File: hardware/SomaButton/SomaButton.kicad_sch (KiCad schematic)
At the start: 18 parts, among them J1 LED+, J2 LED GND, J3 BTN GND, J4 I2C, J5 V12, J6 Buttons, J7 V5, U2 ULN2803A, U3 ULN2803A

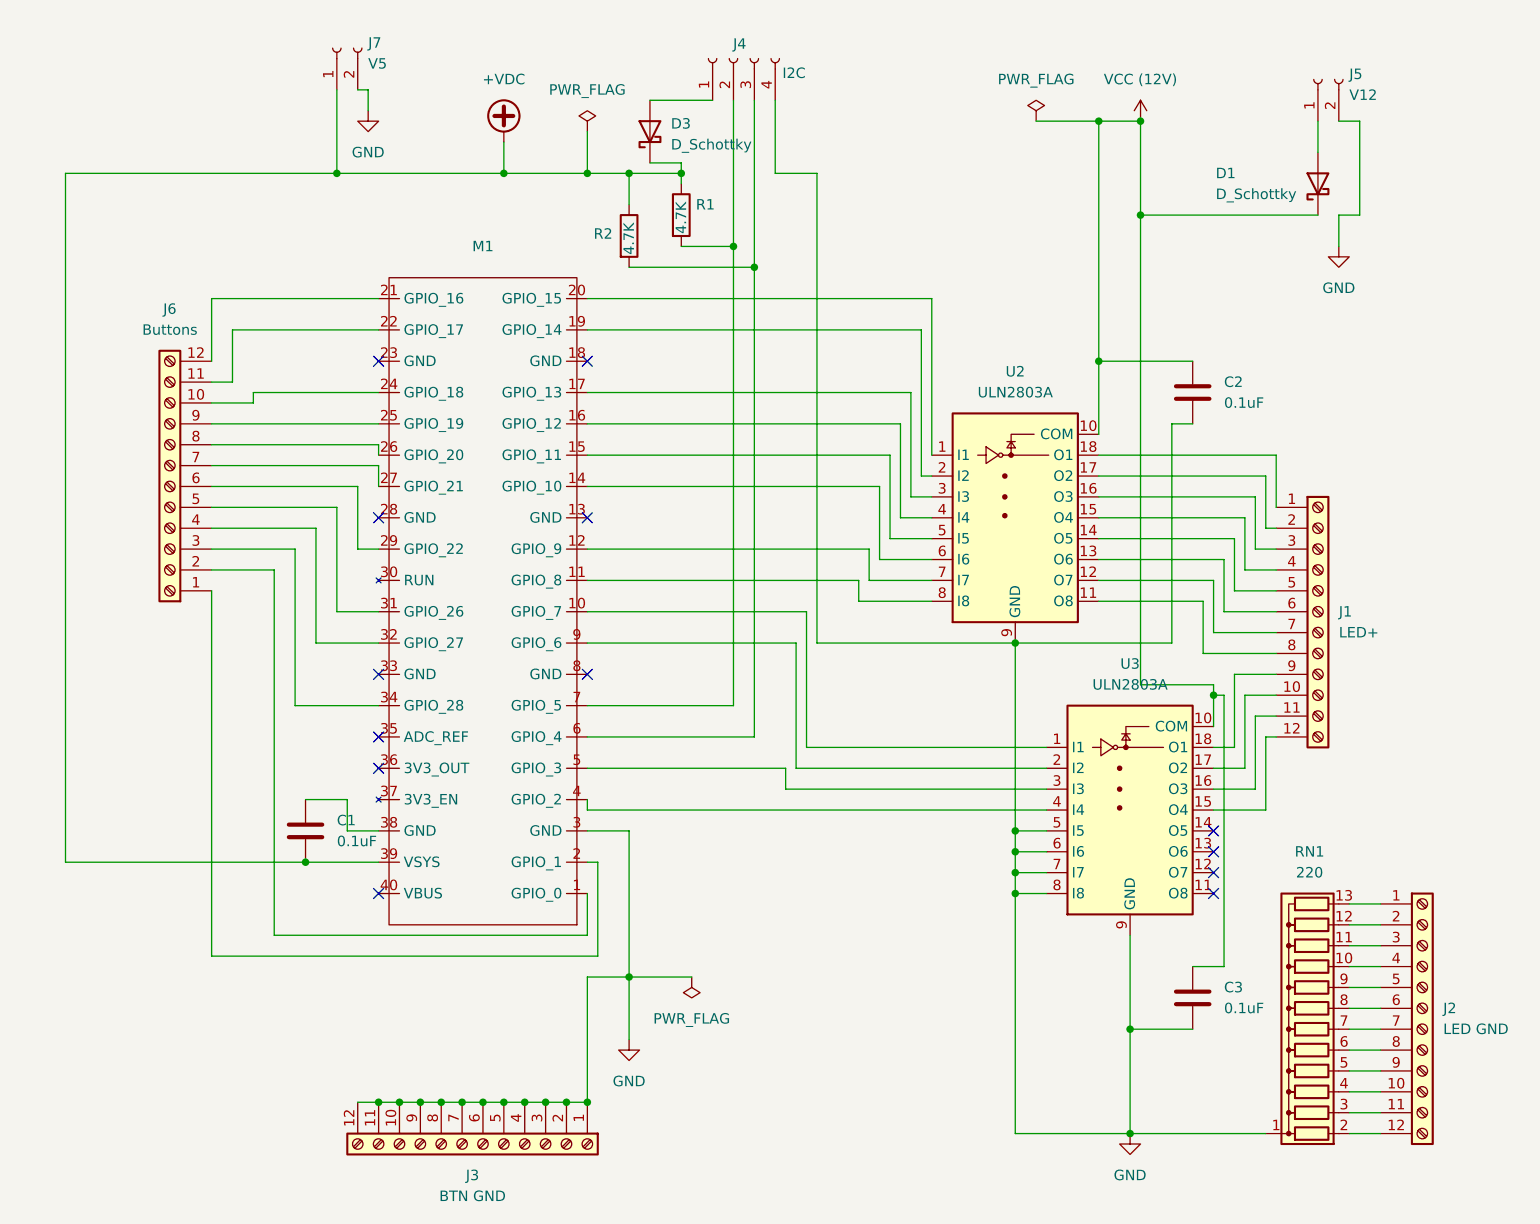
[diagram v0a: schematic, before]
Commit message: hardware: combo board, LED board, production outputs, arduino firmware
Co-Authored-By: Claude Opus 5.5 (1M context) <noreply@anthropic.com>
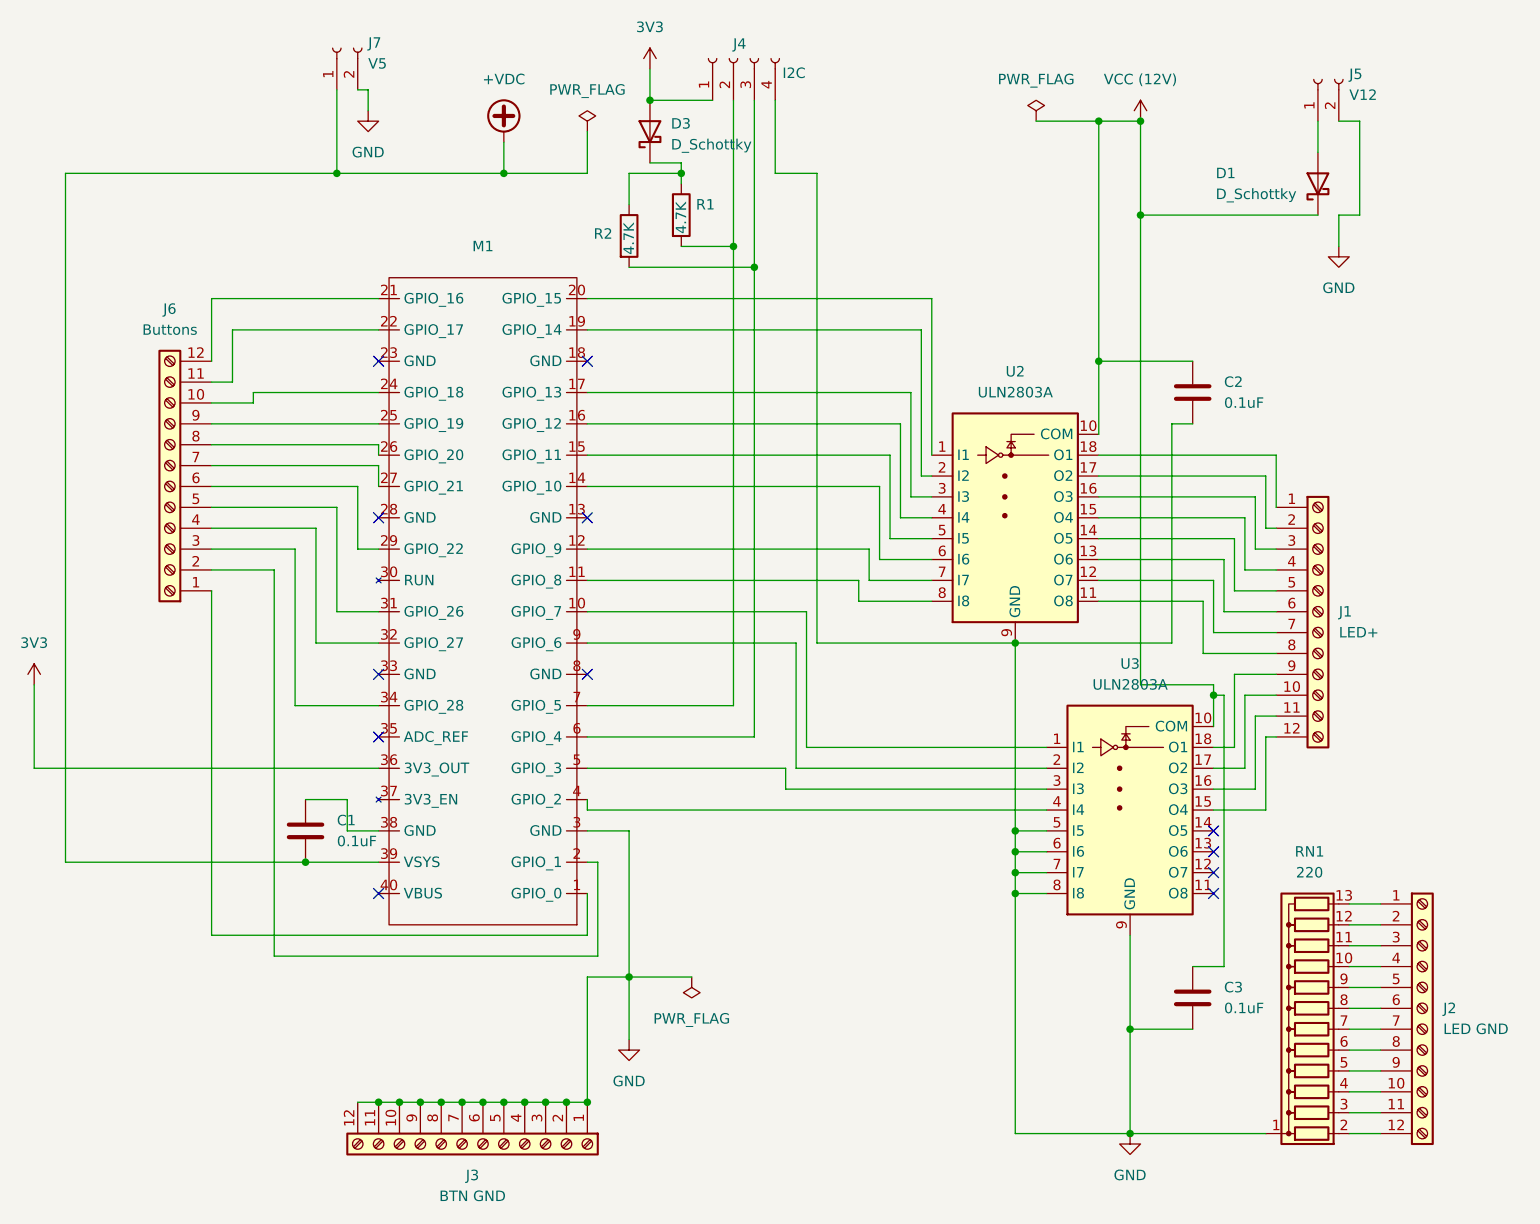
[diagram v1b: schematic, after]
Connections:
- net +VDC: no longer D3.1 (K), R1.1, R2.1
- net at M1.1 (GPIO_0): now also J6.1 (Pin_1); no longer J6.2 (Pin_2)
- net at M1.2 (GPIO_1): now also J6.2 (Pin_2); no longer J6.1 (Pin_1)
- net 3V3: now reaches M1.36 (3V3_OUT)
- net 3V3: now also D3.2 (A), J4.1 (Pin_1)
- new net: D3.1 (K), R1.1, R2.1
- no-connect marks 13 -> 12
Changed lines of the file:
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@@
 	)
 	(junction
-		(at 114.3 31.75)
-		(diameter 0)
-		(color 0 0 0 0)
-	)
-	(junction
 		(at 170.18 25.4)
 		(diameter 0)
@@
 	)
 	(junction
-		(at 102.87 31.75)
+		(at 80.01 144.78)
 		(diameter 0)
 		(color 0 0 0 0)
 	)
 	(junction
-		(at 80.01 144.78)
+		(at 154.94 88.9)
 		(diameter 0)
 		(color 0 0 0 0)
 	)
 	(junction
-		(at 154.94 88.9)
+		(at 110.49 22.86)
 		(diameter 0)
 		(color 0 0 0 0)
@@
 	)
 	(junction
+		(at 114.3 31.75)
+		(diameter 0)
+		(color 0 0 0 0)
+	)
+	(junction
 		(at 92.71 144.78)
 		(diameter 0)
@@
 	)
 	(junction
-		(at 107.95 31.75)
-		(diameter 0)
-		(color 0 0 0 0)
-	)
-	(junction
 		(at 168.91 135.89)
 		(diameter 0)
@@
 	)
 	(no_connect
-		(at 77.47 104.14)
-	)
-	(no_connect
 		(at 102.87 92.71)
 	)
@@
 	(wire
 		(pts
+			(xy 57.15 124.46) (xy 102.87 124.46)
+		)
+		(stroke
+			(width 0)
+			(type default)
+		)
+	)
+	(wire
+		(pts
 			(xy 165.1 78.74) (xy 180.34 78.74)
 		)
@@
 	(wire
 		(pts
-			(xy 102.87 31.75) (xy 107.95 31.75)
-		)
-		(stroke
-			(width 0)
-			(type default)
-		)
-	)
-	(wire
-		(pts
 			(xy 57.15 72.39) (xy 72.39 72.39)
 		)
@@
 	(wire
 		(pts
-			(xy 114.3 31.75) (xy 114.3 33.02)
+			(xy 114.3 30.48) (xy 114.3 31.75)
 		)
 		(stroke
@@
 	(wire
 		(pts
-			(xy 57.15 82.55) (xy 57.15 127)
-		)
-		(stroke
-			(width 0)
-			(type default)
-		)
-	)
-	(wire
-		(pts
 			(xy 120.65 96.52) (xy 120.65 40.64)
 		)
@@
 	(wire
 		(pts
-			(xy 64.77 80.01) (xy 64.77 124.46)
+			(xy 67.31 96.52) (xy 77.47 96.52)
 		)
 		(stroke
@@
 	(wire
 		(pts
-			(xy 67.31 96.52) (xy 77.47 96.52)
+			(xy 176.53 62.23) (xy 173.99 62.23)
 		)
 		(stroke
@@
 	(wire
 		(pts
-			(xy 176.53 62.23) (xy 173.99 62.23)
+			(xy 168.91 148.59) (xy 185.42 148.59)
 		)
 		(stroke
@@
 	(wire
 		(pts
-			(xy 168.91 148.59) (xy 185.42 148.59)
+			(xy 110.49 19.05) (xy 110.49 22.86)
 		)
 		(stroke
@@
 	(wire
 		(pts
+			(xy 107.95 31.75) (xy 114.3 31.75)
+		)
+		(stroke
+			(width 0)
+			(type default)
+		)
+	)
+	(wire
+		(pts
 			(xy 74.93 144.78) (xy 77.47 144.78)
 		)
@@
 	(wire
 		(pts
+			(xy 114.3 31.75) (xy 114.3 33.02)
+		)
+		(stroke
+			(width 0)
+			(type default)
+		)
+	)
+	(wire
+		(pts
 			(xy 195.58 143.51) (xy 199.39 143.51)
 		)
@@
 	(wire
 		(pts
-			(xy 107.95 31.75) (xy 114.3 31.75)
+			(xy 35.56 93.98) (xy 35.56 104.14)
 		)
 		(stroke
@@
 	(wire
 		(pts
+			(xy 77.47 104.14) (xy 35.56 104.14)
+		)
+		(stroke
+			(width 0)
+			(type default)
+		)
+	)
+	(wire
+		(pts
 			(xy 130.81 88.9) (xy 154.94 88.9)
 		)
@@
 	(wire
 		(pts
-			(xy 104.14 127) (xy 57.15 127)
+			(xy 104.14 127) (xy 64.77 127)
 		)
 		(stroke
@@
 	(wire
 		(pts
-			(xy 102.87 124.46) (xy 64.77 124.46)
-		)
-		(stroke
-			(width 0)
-			(type default)
-		)
-	)
-	(wire
-		(pts
 			(xy 180.34 95.25) (xy 179.07 95.25)
 		)
@@
 	(wire
 		(pts
+			(xy 64.77 80.01) (xy 64.77 127)
+		)
+		(stroke
+			(width 0)
+			(type default)
+		)
+	)
+	(wire
+		(pts
 			(xy 57.15 62.23) (xy 77.47 62.23)
 		)
@@
 	(wire
 		(pts
-			(xy 114.3 30.48) (xy 114.3 31.75)
-		)
-		(stroke
-			(width 0)
-			(type default)
-		)
-	)
-	(wire
-		(pts
 			(xy 140.97 62.23) (xy 102.87 62.23)
 		)
@@
 	(wire
 		(pts
+			(xy 57.15 124.46) (xy 57.15 82.55)
+		)
+		(stroke
+			(width 0)
+			(type default)
+		)
+	)
+	(wire
+		(pts
 			(xy 59.69 50.8) (xy 77.47 50.8)
 		)
@@
 	)
 	(symbol
+		(lib_id "power:VCC")
+		(at 110.49 19.05 0)
+		(unit 1)
+		(exclude_from_sim no)
+		(in_bom yes)
+		(on_board yes)
+		(dnp no)
+		(fields_autoplaced yes)
+		(property "Reference" "#PWR08"
+			(at 110.49 22.86 0)
+			(effects
+				(font
+					(size 1.27 1.27)
+				)
+				(hide yes)
+			)
+		)
+		(property "Value" "3V3"
+			(at 110.49 13.97 0)
+			(effects
+				(font
+					(size 1.27 1.27)
+				)
+			)
+		)
+		(property "Footprint" ""
+			(at 110.49 19.05 0)
+			(effects
+				(font
+					(size 1.27 1.27)
+				)
+				(hide yes)
+			)
+		)
+		(property "Datasheet" ""
+			(at 110.49 19.05 0)
+			(effects
+				(font
+					(size 1.27 1.27)
+				)
+				(hide yes)
+			)
+		)
+		(property "Description" "Power symbol creates a global label with name \"VCC\""
+			(at 110.49 19.05 0)
+			(effects
+				(font
+					(size 1.27 1.27)
+				)
+				(hide yes)
+			)
+		)
+		(pin "1"
+		)
+		(instances
+			(project "SomaButton"
+				(path "/7f241255-1ca6-421f-be92-420475f0c4c4"
+					(reference "#PWR08")
+					(unit 1)
+				)
+			)
+		)
+	)
+	(symbol
 		(lib_id "Transistor_Array:ULN2803A")
 		(at 154.94 71.12 0)
@@
 					(unit 1)
 				)
+			)
+		)
+	)
+	(symbol
+		(lib_id "power:VCC")
+		(at 35.56 93.98 0)
+		(unit 1)
+		(exclude_from_sim no)
+		(in_bom yes)
+		(on_board yes)
+		(dnp no)
+		(fields_autoplaced yes)
+		(property "Reference" "#PWR07"
+			(at 35.56 97.79 0)
+			(effects
+				(font
+					(size 1.27 1.27)
+				)
+				(hide yes)
+			)
+		)
+		(property "Value" "3V3"
+			(at 35.56 88.9 0)
+			(effects
+				(font
+					(size 1.27 1.27)
+				)
+			)
+		)
+		(property "Footprint" ""
+			(at 35.56 93.98 0)
+			(effects
+				(font
+					(size 1.27 1.27)
+				)
+				(hide yes)
+			)
+		)
+		(property "Datasheet" ""
+			(at 35.56 93.98 0)
+			(effects
+				(font
+					(size 1.27 1.27)
+				)
+				(hide yes)
+			)
+		)
+		(property "Description" "Power symbol creates a global label with name \"VCC\""
+			(at 35.56 93.98 0)
+			(effects
+				(font
+					(size 1.27 1.27)
+				)
+				(hide yes)
+			)
+		)
+		(pin "1"
+		)
+		(instances
+			(project ""
+				(path "/7f241255-1ca6-421f-be92-420475f0c4c4"
+					(reference "#PWR07")
+					(unit 1)
+				)
